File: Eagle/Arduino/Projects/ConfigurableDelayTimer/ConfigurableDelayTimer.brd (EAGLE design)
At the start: 100 x 80 mm, 20 parts

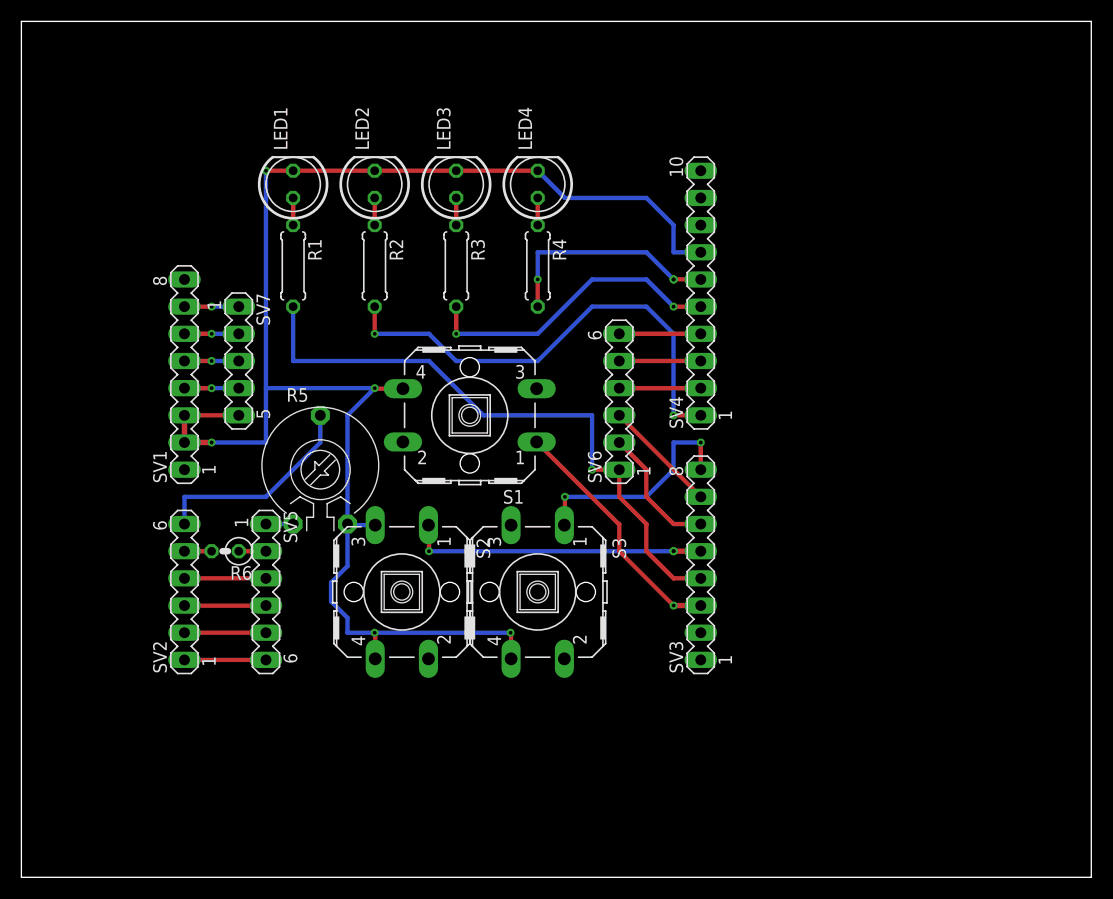
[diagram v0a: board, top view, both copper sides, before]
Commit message: changed schematics - Measurement of current
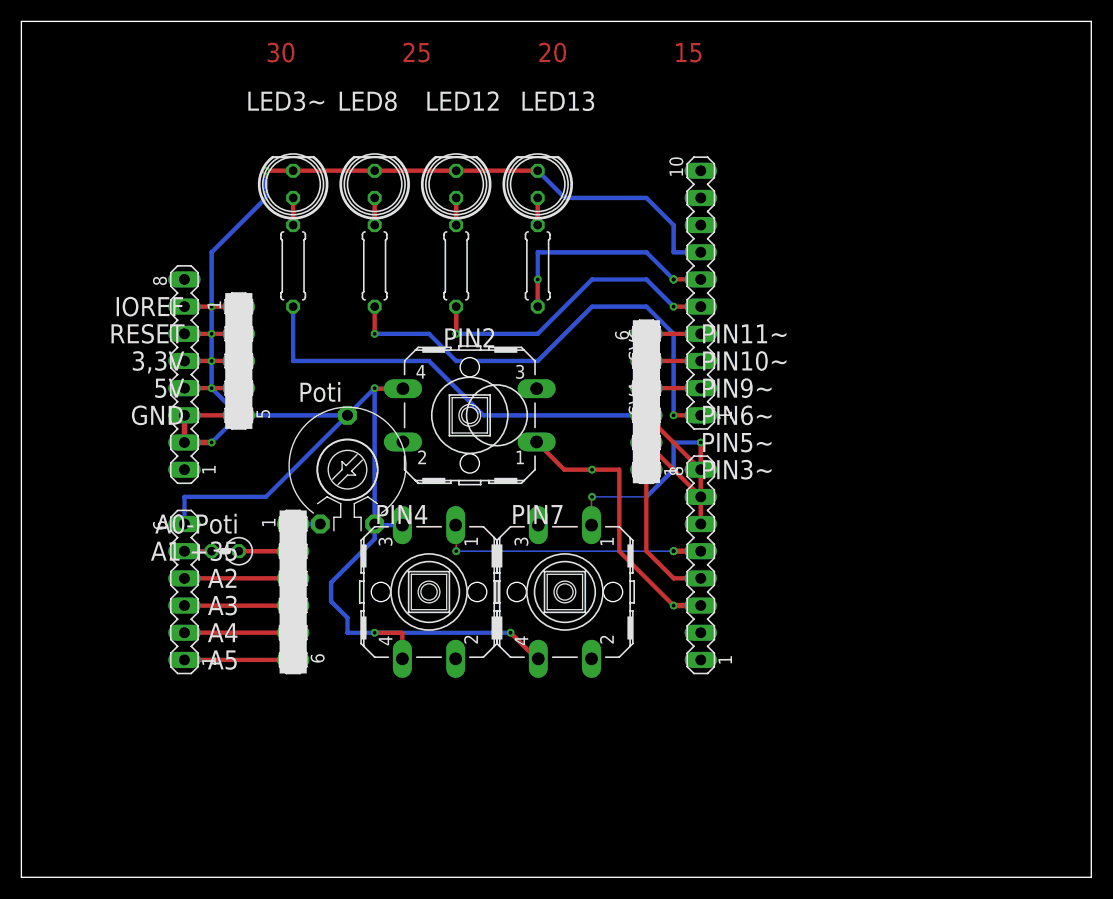
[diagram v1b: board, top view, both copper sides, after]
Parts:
- moved R5 2.54 mm to (30.5, 38.1)
- moved S2 2.54 mm to (38.1, 26.7)
- moved S3 2.54 mm to (50.8, 26.7)
- moved SV5 2.54 mm to (25.4, 26.7)
- moved SV6 2.54 mm to (58.4, 44.5)
- renumbered LED1 to LED3~, LED2 to LED8, LED3 to LED12, LED4 to LED13
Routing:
- net GND: track 146.9 -> 153.3 mm
- net PIN2: track 23.2 -> 26.1 mm
- net PIN4: track 28.0 -> 25.3 mm
- net PIN9~: track 7.62 -> 5.08 mm
- net PIN5~: track 12.3 -> 9.72 mm
- net PIN11~: track 7.62 -> 5.08 mm
- net PIN10~: track 7.62 -> 5.08 mm
- net N$8: track 2.54 -> 5.08 mm
- net A5: track 7.62 -> 10.2 mm
- net A4: track 7.62 -> 10.2 mm
- net A3: track 7.62 -> 10.2 mm
- net A2: track 7.62 -> 10.2 mm
- net PIN7: track 21.5 -> 19.0 mm
- net PIN3~: track 57.5 -> 59.0 mm
- net PIN6~: track 10.8 -> 9.72 mm
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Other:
- board text added: "15"
- board text added: "20"
- board text added: "25"
- board text added: "3,3V"
- board text added: "30"
- board text added: "5V"
- board text added: "A0-Poti"
- board text added: "A1 +35"
- board text added: "A2"
- board text added: "A3"
- board text added: "A4"
- board text added: "A5"
- board text added: "GND"
- board text added: "IOREF"
- board text added: "PIN10~"
- board text added: "PIN11~"
- board text added: "PIN2"
- board text added: "PIN3~"
- board text added: "PIN4"
- board text added: "PIN5~"
- board text added: "PIN6~"
- board text added: "PIN7"
- board text added: "PIN9~"
- board text added: "Poti"
- board text added: "RESET"
